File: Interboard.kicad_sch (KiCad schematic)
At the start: 1 part

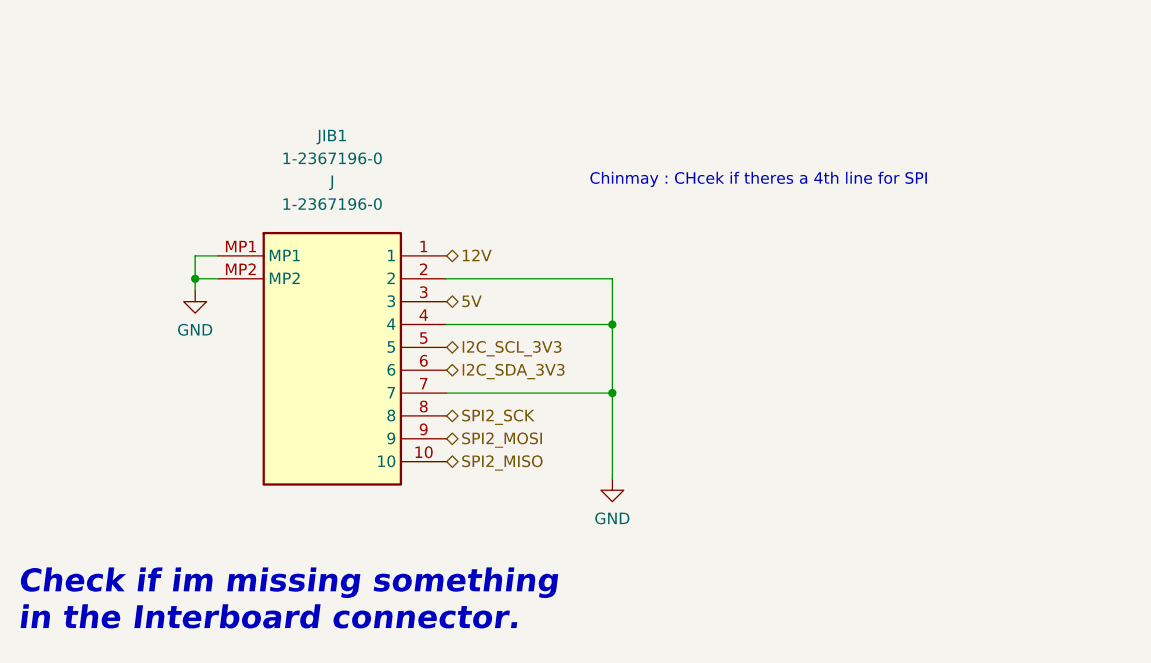
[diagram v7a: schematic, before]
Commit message: I2C lines are pulled up
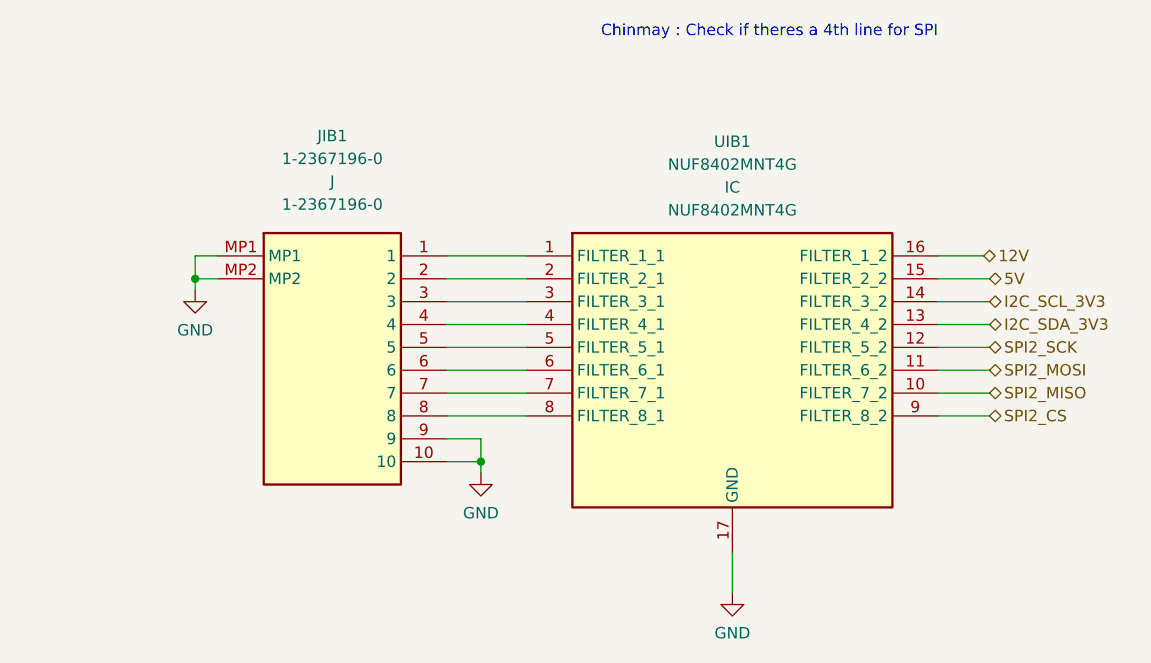
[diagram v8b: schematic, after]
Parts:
- added UIB1: NUF8402MNT4G, NUF8402MNT4G:SON50P160X400X100-17N, symbol NUF8402MNT4G:NUF8402MNT4G
- JIB1: footprint (none) -> 1-2367196-0:123671960
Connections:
- net 12V: now also UIB1.16 (FILTER_1_2); no longer JIB1.1
- net 5V: now also UIB1.15 (FILTER_2_2); no longer JIB1.3
- net GND: now also JIB1.10, JIB1.9, UIB1.17 (GND); no longer JIB1.2, JIB1.4, JIB1.7
- net I2C_SCL_3V3: now also UIB1.14 (FILTER_3_2); no longer JIB1.5
- net I2C_SDA_3V3: now also UIB1.13 (FILTER_4_2); no longer JIB1.6
- net SPI2_MISO: now also UIB1.10 (FILTER_7_2); no longer JIB1.10
- net SPI2_MOSI: now also UIB1.11 (FILTER_6_2); no longer JIB1.9
- net SPI2_SCK: now also UIB1.12 (FILTER_5_2); no longer JIB1.8
- new net: JIB1.1, UIB1.1 (FILTER_1_1)
- new net: JIB1.2, UIB1.2 (FILTER_2_1)
- new net: JIB1.3, UIB1.3 (FILTER_3_1)
- new net: JIB1.4, UIB1.4 (FILTER_4_1)
- new net: JIB1.5, UIB1.5 (FILTER_5_1)
- new net: JIB1.6, UIB1.6 (FILTER_6_1)
- new net: JIB1.7, UIB1.7 (FILTER_7_1)
- new net: JIB1.8, UIB1.8 (FILTER_8_1)
- new net SPI2_CS: UIB1.9 (FILTER_8_2)
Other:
- note added: "Chinmay : Check if theres a 4th line for SPI"
- note removed: "Check if im missing something in the Interboard connector."
- note removed: "Chinmay : CHcek if theres a 4th line for SPI"
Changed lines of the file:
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@@
   (junction (at 121.285 76.2) (diameter 0) (color 0 0 0 0)
   )
-  (junction (at 167.64 88.9) (diameter 0) (color 0 0 0 0)
-  )
-  (junction (at 167.64 81.28) (diameter 0) (color 0 0 0 0)
+  (junction (at 153.035 96.52) (diameter 0) (color 0 0 0 0)
+  )
+  (wire (pts (xy 203.835 81.28) (xy 209.55 81.28))
+    (stroke (width 0) (type default) (color 0 0 0 0))
+  )
+  (wire (pts (xy 149.225 96.52) (xy 153.035 96.52))
+    (stroke (width 0) (type default) (color 0 0 0 0))
+  )
+  (wire (pts (xy 203.835 91.44) (xy 209.55 91.44))
+    (stroke (width 0) (type default) (color 0 0 0 0))
   )
   (wire (pts (xy 121.285 76.2) (xy 121.285 77.47))
     (stroke (width 0) (type default) (color 0 0 0 0))
   )
-  (wire (pts (xy 149.225 76.2) (xy 167.64 76.2))
-    (stroke (width 0) (type default) (color 0 0 0 0))
-  )
-  (wire (pts (xy 167.64 76.2) (xy 167.64 81.28))
-    (stroke (width 0) (type default) (color 0 0 0 0))
-  )
-  (wire (pts (xy 167.64 88.9) (xy 167.64 98.425))
-    (stroke (width 0) (type default) (color 0 0 0 0))
-  )
-  (wire (pts (xy 167.64 81.28) (xy 167.64 88.9))
-    (stroke (width 0) (type default) (color 0 0 0 0))
-  )
-  (wire (pts (xy 149.225 81.28) (xy 167.64 81.28))
+  (wire (pts (xy 203.835 78.74) (xy 209.55 78.74))
+    (stroke (width 0) (type default) (color 0 0 0 0))
+  )
+  (wire (pts (xy 153.035 93.98) (xy 153.035 96.52))
+    (stroke (width 0) (type default) (color 0 0 0 0))
+  )
+  (wire (pts (xy 149.225 76.2) (xy 158.115 76.2))
+    (stroke (width 0) (type default) (color 0 0 0 0))
+  )
+  (wire (pts (xy 149.225 83.82) (xy 158.115 83.82))
+    (stroke (width 0) (type default) (color 0 0 0 0))
+  )
+  (wire (pts (xy 149.225 88.9) (xy 158.115 88.9))
+    (stroke (width 0) (type default) (color 0 0 0 0))
+  )
+  (wire (pts (xy 149.225 86.36) (xy 158.115 86.36))
+    (stroke (width 0) (type default) (color 0 0 0 0))
+  )
+  (wire (pts (xy 149.225 73.66) (xy 158.115 73.66))
+    (stroke (width 0) (type default) (color 0 0 0 0))
+  )
+  (wire (pts (xy 149.225 91.44) (xy 158.115 91.44))
+    (stroke (width 0) (type default) (color 0 0 0 0))
+  )
+  (wire (pts (xy 180.975 106.68) (xy 180.975 111.125))
+    (stroke (width 0) (type default) (color 0 0 0 0))
+  )
+  (wire (pts (xy 153.035 96.52) (xy 153.035 97.79))
+    (stroke (width 0) (type default) (color 0 0 0 0))
+  )
+  (wire (pts (xy 203.835 83.82) (xy 209.55 83.82))
+    (stroke (width 0) (type default) (color 0 0 0 0))
+  )
+  (wire (pts (xy 149.225 81.28) (xy 158.115 81.28))
     (stroke (width 0) (type default) (color 0 0 0 0))
   )
@@
     (stroke (width 0) (type default) (color 0 0 0 0))
   )
+  (wire (pts (xy 203.835 88.9) (xy 209.55 88.9))
+    (stroke (width 0) (type default) (color 0 0 0 0))
+  )
   (wire (pts (xy 121.285 73.66) (xy 121.285 76.2))
     (stroke (width 0) (type default) (color 0 0 0 0))
   )
-  (wire (pts (xy 149.225 88.9) (xy 167.64 88.9))
-    (stroke (width 0) (type default) (color 0 0 0 0))
-  )
-  (text "Check if im missing something\nin the Interboard connector."
-    (at 101.6 115.57 0)
-    (effects (font (size 2.54 2.54) (thickness 0.508) bold italic) (justify left bottom))
-  )
-  (text "Chinmay : CHcek if theres a 4th line for SPI " (at 165.1 66.04 0)
+  (wire (pts (xy 203.835 86.36) (xy 209.55 86.36))
+    (stroke (width 0) (type default) (color 0 0 0 0))
+  )
+  (wire (pts (xy 149.225 78.74) (xy 158.115 78.74))
+    (stroke (width 0) (type default) (color 0 0 0 0))
+  )
+  (wire (pts (xy 149.225 93.98) (xy 153.035 93.98))
+    (stroke (width 0) (type default) (color 0 0 0 0))
+  )
+  (wire (pts (xy 203.835 76.2) (xy 209.55 76.2))
+    (stroke (width 0) (type default) (color 0 0 0 0))
+  )
+  (wire (pts (xy 203.835 73.66) (xy 208.915 73.66))
+    (stroke (width 0) (type default) (color 0 0 0 0))
+  )
+  (text "Chinmay : Check if theres a 4th line for SPI " (at 166.37 49.53 0)
     (effects (font (size 1.27 1.27)) (justify left bottom))
   )
-  (hierarchical_label "5V" (shape bidirectional) (at 149.225 78.74 0)
-    (effects (font (size 1.27 1.27)) (justify left))
-  )
-  (hierarchical_label "12V" (shape bidirectional) (at 149.225 73.66 0)
-    (effects (font (size 1.27 1.27)) (justify left))
-  )
-  (hierarchical_label "I2C_SCL_3V3" (shape bidirectional) (at 149.225 83.82 0)
-    (effects (font (size 1.27 1.27)) (justify left))
-  )
-  (hierarchical_label "SPI2_MOSI" (shape bidirectional) (at 149.225 93.98 0)
-    (effects (font (size 1.27 1.27)) (justify left))
-  )
-  (hierarchical_label "SPI2_SCK" (shape bidirectional) (at 149.225 91.44 0)
-    (effects (font (size 1.27 1.27)) (justify left))
-  )
-  (hierarchical_label "I2C_SDA_3V3" (shape bidirectional) (at 149.225 86.36 0)
-    (effects (font (size 1.27 1.27)) (justify left))
-  )
-  (hierarchical_label "SPI2_MISO" (shape bidirectional) (at 149.225 96.52 0)
+  (hierarchical_label "5V" (shape bidirectional) (at 209.55 76.2 0)
+    (effects (font (size 1.27 1.27)) (justify left))
+  )
+  (hierarchical_label "12V" (shape bidirectional) (at 208.915 73.66 0)
+    (effects (font (size 1.27 1.27)) (justify left))
+  )
+  (hierarchical_label "I2C_SCL_3V3" (shape bidirectional) (at 209.55 78.74 0)
+    (effects (font (size 1.27 1.27)) (justify left))
+  )
+  (hierarchical_label "SPI2_MOSI" (shape bidirectional) (at 209.55 86.36 0)
+    (effects (font (size 1.27 1.27)) (justify left))
+  )
+  (hierarchical_label "SPI2_SCK" (shape bidirectional) (at 209.55 83.82 0)
+    (effects (font (size 1.27 1.27)) (justify left))
+  )
+  (hierarchical_label "I2C_SDA_3V3" (shape bidirectional) (at 209.55 81.28 0)
+    (effects (font (size 1.27 1.27)) (justify left))
+  )
+  (hierarchical_label "SPI2_CS" (shape bidirectional) (at 209.55 91.44 0)
+    (effects (font (size 1.27 1.27)) (justify left))
+  )
+  (hierarchical_label "SPI2_MISO" (shape bidirectional) (at 209.55 88.9 0)
     (effects (font (size 1.27 1.27)) (justify left))
   )
@@
     (property "Reference" "JIB1" (id 0) (at 136.525 60.325 0))
     (property "Value" "1-2367196-0" (id 1) (at 136.525 62.865 0))
-    (property "Footprint" "" (id 2) (at 123.825 73.66 0)
+    (property "Footprint" "1-2367196-0:123671960" (id 2) (at 123.825 73.66 0)
       (effects (font (size 1.27 1.27)) hide)
     )
@@
   (symbol (lib_id "upsat-comms-hardware:GND") (at 121.285 77.47 0) (unit 1)
     (in_bom yes) (on_board yes) (fields_autoplaced)
-    (property "Reference" "#PWR0161" (id 0) (at 121.285 83.82 0)
+    (property "Reference" "#PWR0162" (id 0) (at 121.285 83.82 0)
       (effects (font (size 1.27 1.27)) hide)
     )
@@
     (pin "1")
   )
-  (symbol (lib_id "upsat-comms-hardware:GND") (at 167.64 98.425 0) (unit 1)
-    (in_bom yes) (on_board yes) (fields_autoplaced)
-    (property "Reference" "#PWR0162" (id 0) (at 167.64 104.775 0)
-      (effects (font (size 1.27 1.27)) hide)
-    )
-    (property "Value" "GND" (id 1) (at 167.64 102.87 0))
-    (property "Footprint" "" (id 2) (at 167.64 98.425 0))
-    (property "Datasheet" "" (id 3) (at 167.64 98.425 0))
-    (pin "1")
-  )
+  (symbol (lib_id "upsat-comms-hardware:GND") (at 153.035 97.79 0) (unit 1)
+    (in_bom yes) (on_board yes) (fields_autoplaced)
+    (property "Reference" "#PWR0163" (id 0) (at 153.035 104.14 0)
+      (effects (font (size 1.27 1.27)) hide)
+    )
+    (property "Value" "GND" (id 1) (at 153.035 102.235 0))
+    (property "Footprint" "" (id 2) (at 153.035 97.79 0))
+    (property "Datasheet" "" (id 3) (at 153.035 97.79 0))
+    (pin "1")
+  )
+  (symbol (lib_id "NUF8402MNT4G:NUF8402MNT4G") (at 158.115 73.66 0) (unit 1)
+    (in_bom yes) (on_board yes) (fields_autoplaced)
+    (property "Reference" "UIB1" (id 0) (at 180.975 60.96 0))
+    (property "Value" "NUF8402MNT4G" (id 1) (at 180.975 63.5 0))
+    (property "Footprint" "NUF8402MNT4G:SON50P160X400X100-17N" (id 2) (at 158.115 73.66 0)
+      (effects (font (size 1.27 1.27)) hide)
+    )
+    (property "Datasheet" "" (id 3) (at 158.115 73.66 0)
+      (effects (font (size 1.27 1.27)) hide)
+    )
+    (property "Reference_1" "IC" (id 4) (at 180.975 66.04 0))
+    (property "Value_1" "NUF8402MNT4G" (id 5) (at 180.975 68.58 0))
+    (property "Footprint_1" "SON50P160X400X100-17N" (id 6) (at 200.025 168.58 0)
+      (effects (font (size 1.27 1.27)) (justify left top) hide)
+    )
+    (property "Datasheet_1" "http://www.onsemi.com/pub/Collateral/NUF8402MN-D.PDF" (id 7) (at 200.025 268.58 0)
+      (effects (font (size 1.27 1.27)) (justify left top) hide)
+    )
+    (property "Height" "1" (id 8) (at 200.025 468.58 0)
+      (effects (font (size 1.27 1.27)) (justify left top) hide)
+    )
+    (property "Mouser Part Number" "863-NUF8402MNT4G" (id 9) (at 200.025 568.58 0)
+      (effects (font (size 1.27 1.27)) (justify left top) hide)
+    )
+    (property "Mouser Price/Stock" "https://www.mouser.co.uk/ProductDetail/onsemi/NUF8402MNT4G?qs=ZXBb0xZ9WeBtVbB00WX36A%3D%3D" (id 10) (at 200.025 668.58 0)
+      (effects (font (size 1.27 1.27)) (justify left top) hide)
+    )
+    (property "Manufacturer_Name" "onsemi" (id 11) (at 200.025 768.58 0)
+      (effects (font (size 1.27 1.27)) (justify left top) hide)
+    )
+    (property "Manufacturer_Part_Number" "NUF8402MNT4G" (id 12) (at 200.025 868.58 0)
+      (effects (font (size 1.27 1.27)) (justify left top) hide)
+    )
+    (pin "1")
+    (pin "10")
+    (pin "11")
+    (pin "12")
+    (pin "13")
+    (pin "14")
+    (pin "15")
+    (pin "16")
+    (pin "17")
+    (pin "2")
+    (pin "3")
+    (pin "4")
+    (pin "5")
+    (pin "6")
+    (pin "7")
+    (pin "8")
+    (pin "9")
+  )
+  (symbol (lib_id "upsat-comms-hardware:GND") (at 180.975 111.125 0) (unit 1)
+    (in_bom yes) (on_board yes) (fields_autoplaced)
+    (property "Reference" "#PWR0164" (id 0) (at 180.975 117.475 0)
+      (effects (font (size 1.27 1.27)) hide)
+    )
+    (property "Value" "GND" (id 1) (at 180.975 115.57 0))
+    (property "Footprint" "" (id 2) (at 180.975 111.125 0))
+    (property "Datasheet" "" (id 3) (at 180.975 111.125 0))
+    (pin "1")
+  )
